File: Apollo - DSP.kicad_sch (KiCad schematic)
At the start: 27 parts, among them J1 USB_C_Receptacle_USB2.0, U1 NCP115ASN330T2G, U2 NCP115ASN330T2G, U3 USBLC6-2SC6

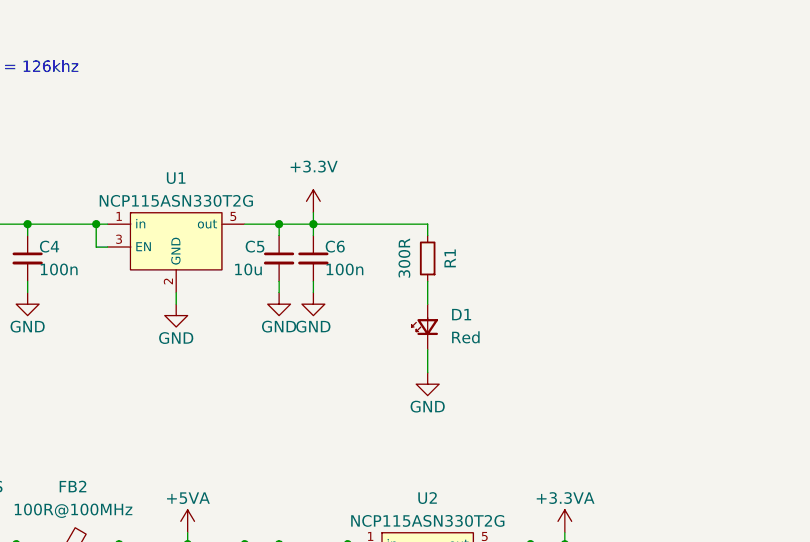
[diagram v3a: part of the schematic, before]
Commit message: added teardrops to increase yield&quality, also tuned usb data line skew
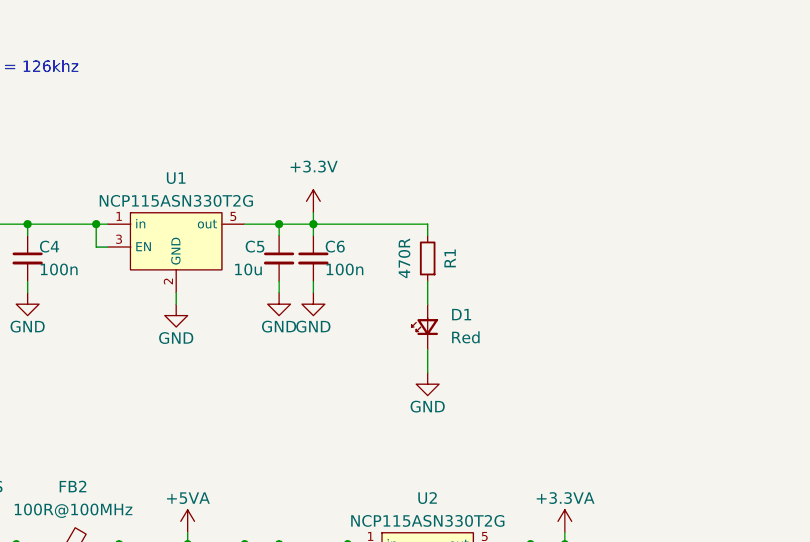
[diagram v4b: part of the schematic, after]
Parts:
- R1: value 300R -> 470R
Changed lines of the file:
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@@
       (effects (font (size 1.27 1.27)))
     )
-    (property "Value" "300R" (at 185.42 73.66 90)
+    (property "Value" "470R" (at 185.42 73.66 90)
       (effects (font (size 1.27 1.27)))
     )

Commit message: modifications for rev 3
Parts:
- removed C10, C12: 100n, Capacitor_SMD:C_0603_1608Metric_Pad1.08x0.95mm_HandSolder, symbol Device:C_Small
- removed C11, C7, C8, C9: 10u, Capacitor_SMD:C_0603_1608Metric_Pad1.08x0.95mm_HandSolder, symbol Device:C_Small
- removed FB2: 100R@100MHz, Resistor_SMD:R_0603_1608Metric_Pad0.98x0.95mm_HandSolder, symbol Device:FerriteBead_Small
- removed U2: NCP115ASN330T2G, NCP115ASN330T2G:NCP115ASN330T2G, symbol NCP115ASN330T2G:NCP115ASN330T2G
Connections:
- net +3.3VA is gone; now on net +3V3: R4.2
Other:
- moved on the sheet: C13, C14, R4, R5

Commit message: ready for order
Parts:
- added C7: 220u, Capacitor_SMD:C_0603_1608Metric_Pad1.08x0.95mm_HandSolder, symbol Device:C_Small
- added C8: 10u, Capacitor_SMD:C_0603_1608Metric_Pad1.08x0.95mm_HandSolder, symbol Device:C_Small
- added L1: 8u8, Inductor_SMD:L_0603_1608Metric_Pad1.05x0.95mm_HandSolder, symbol Device:L_Small
- added R24: 10R, Resistor_SMD:R_0603_1608Metric_Pad0.98x0.95mm_HandSolder, symbol Device:R_Small
- R1: value 470R -> 1k
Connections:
- net +5V: now also R24.1
- net GND: now also C7.2, C8.2
- new net: L1.1, R24.2
- new net +5VA: C7.1, C8.1, L1.2
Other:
- moved on the sheet: C6

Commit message: checking for possible mistakes
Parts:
- U3: footprint SnapEDA Library:SOT95P280X145-6N -> Package_TO_SOT_SMD:SOT-23-6_Handsoldering
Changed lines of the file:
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@@
       (effects (font (size 1.27 1.27)))
     )
-    (property "Footprint" "SnapEDA Library:SOT95P280X145-6N" (at 101.6 134.62 0)
+    (property "Footprint" "Package_TO_SOT_SMD:SOT-23-6_Handsoldering" (at 101.6 134.62 0)
       (effects (font (size 1.27 1.27)) (justify left bottom) hide)
     )
